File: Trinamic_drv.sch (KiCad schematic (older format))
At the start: 26 parts

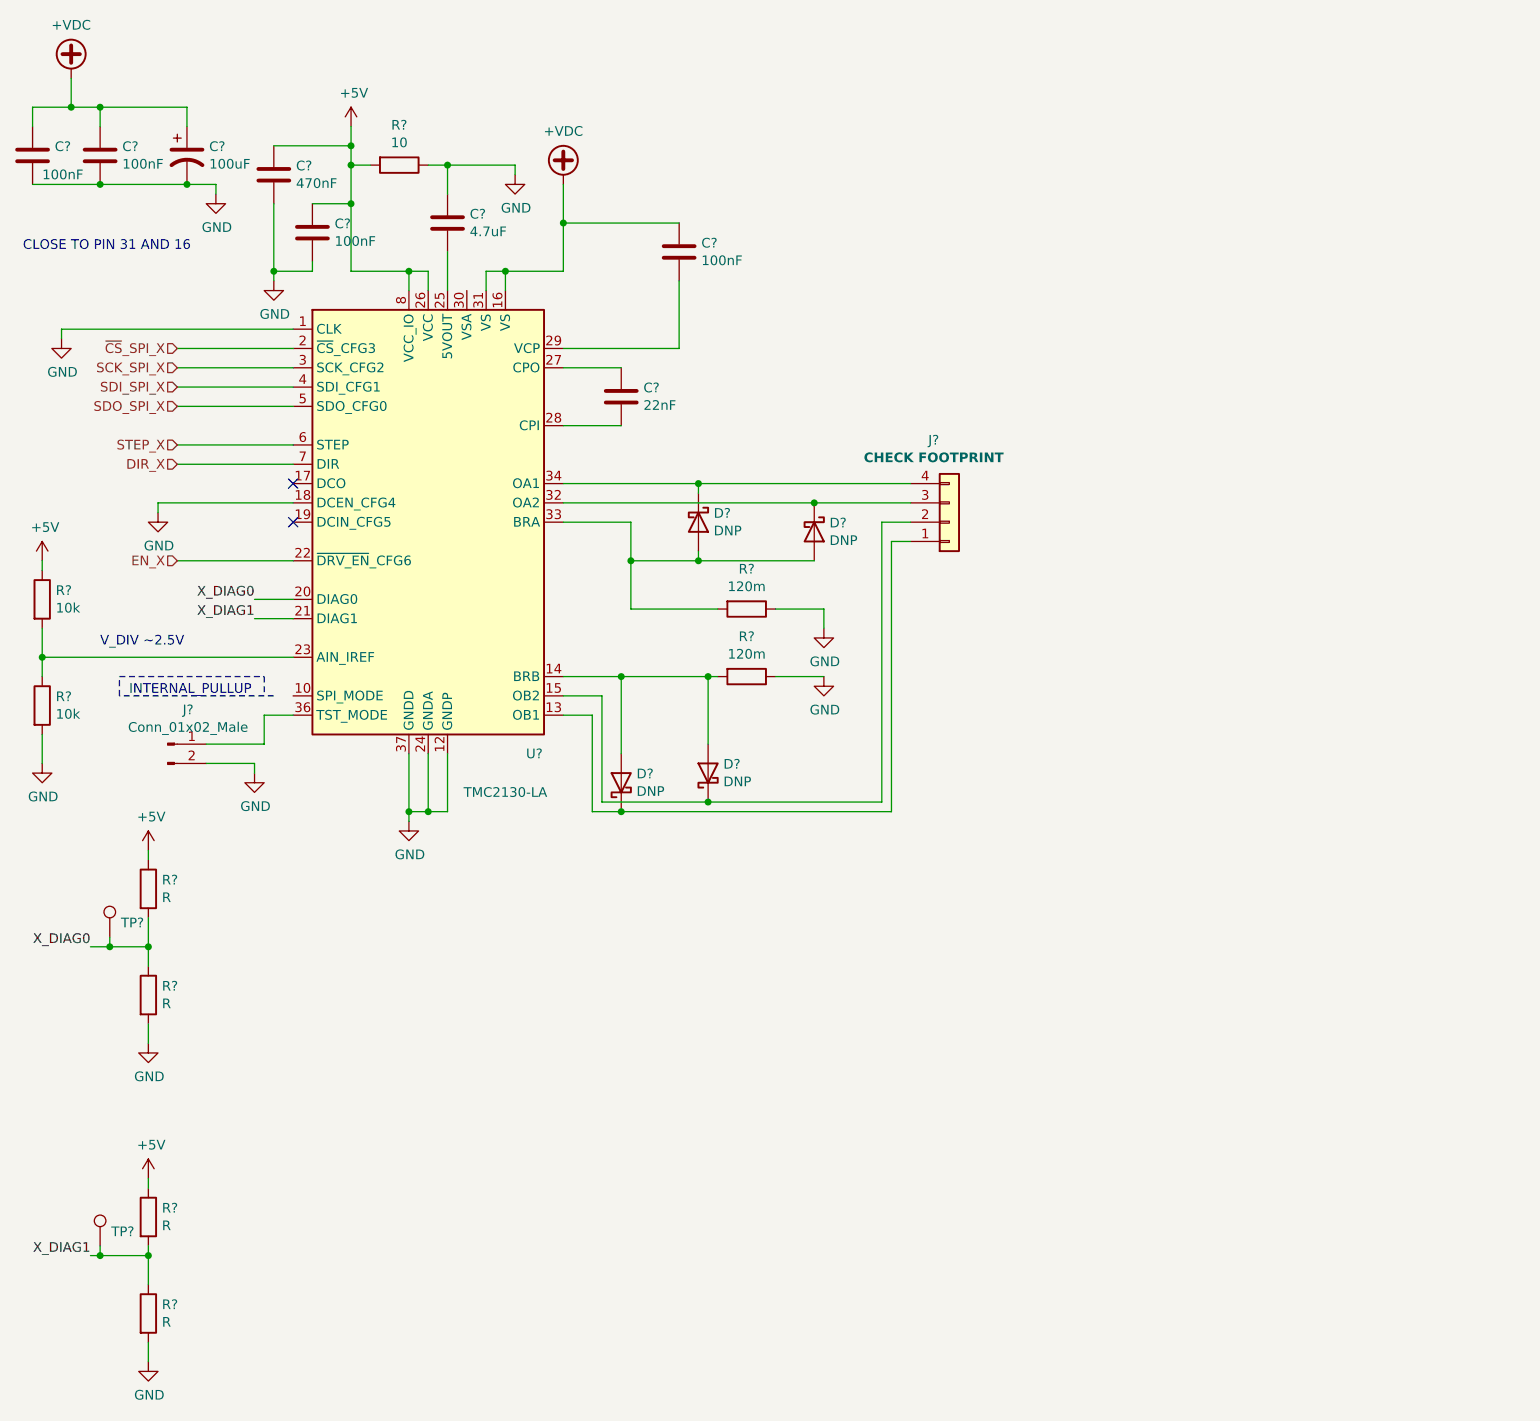
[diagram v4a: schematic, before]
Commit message: Added all stepper circuits. Adding SPI bus to top level sheet. Opened up layout to check connectivity. Errors with footprint libs
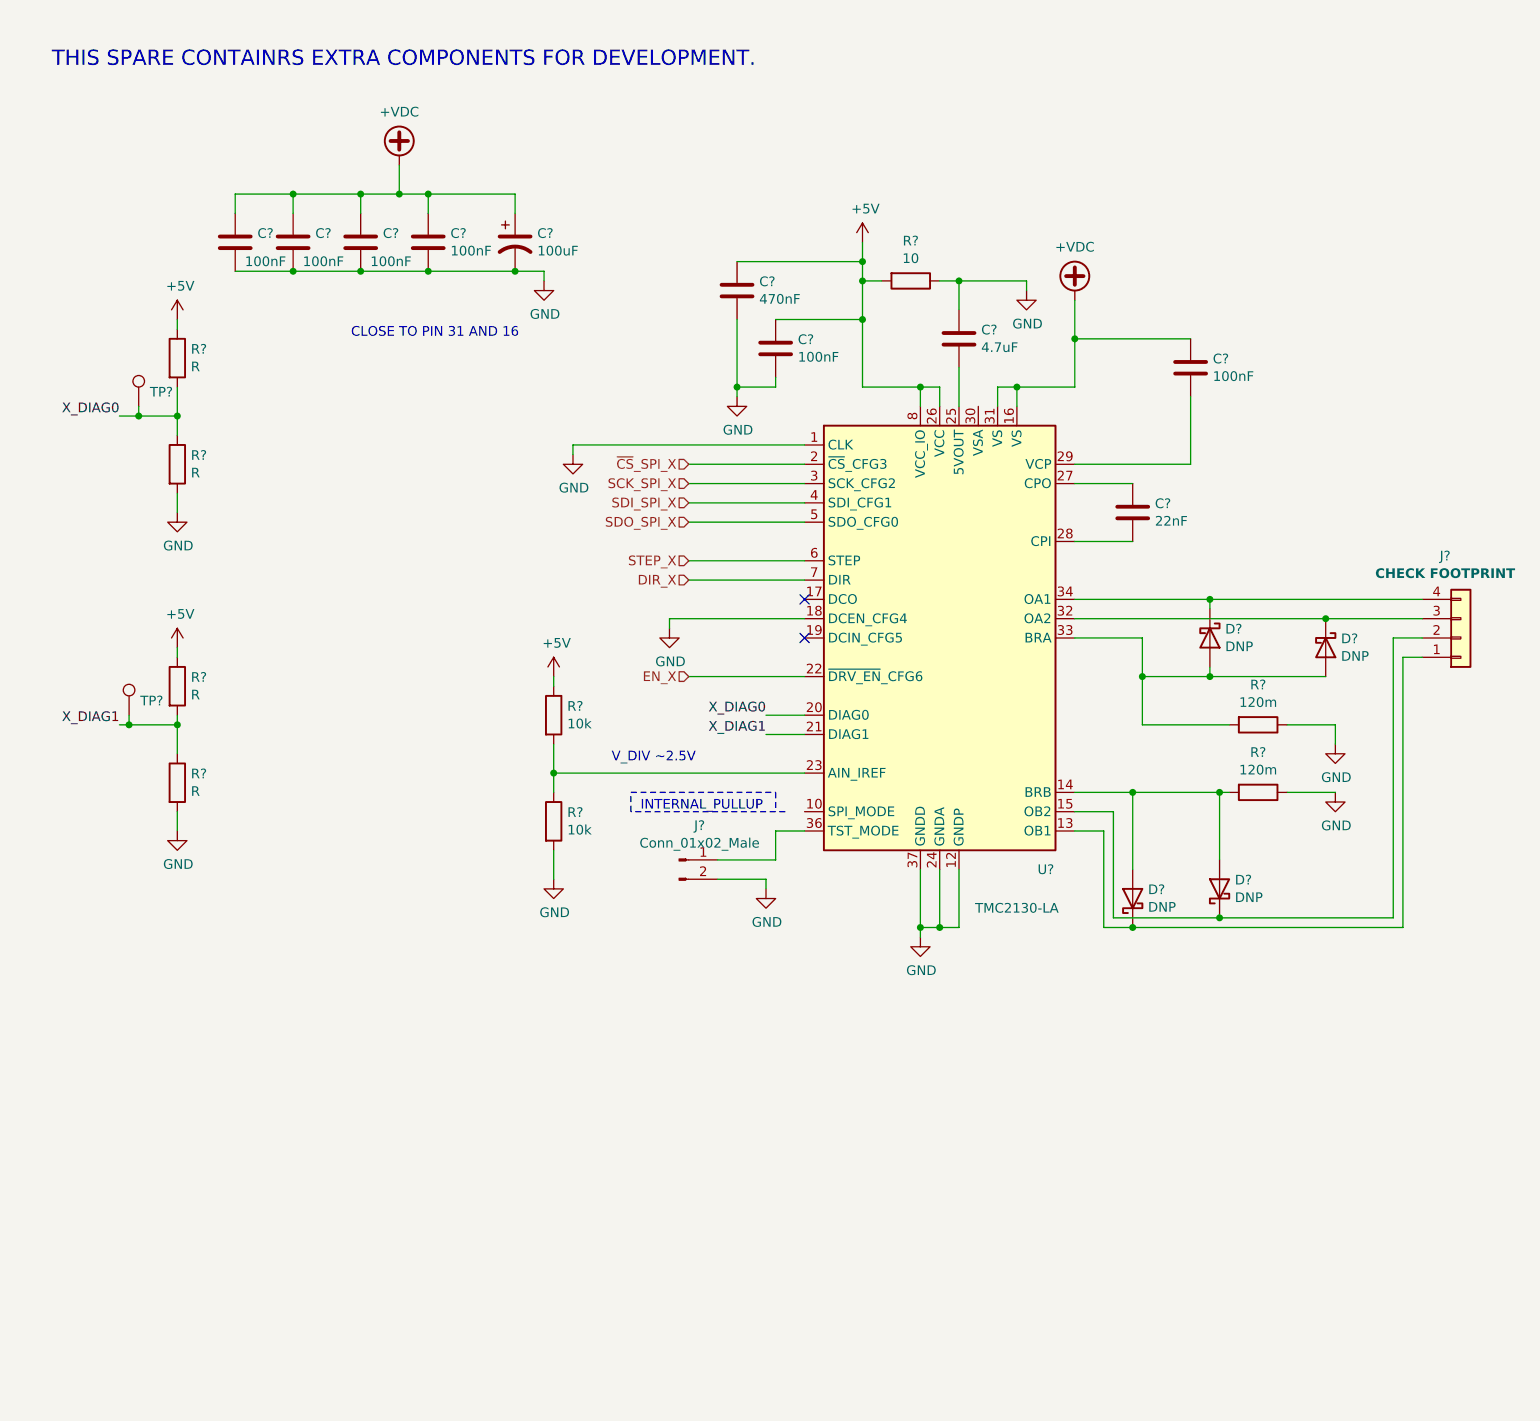
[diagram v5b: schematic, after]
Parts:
- removed R? (x3): R, symbol Device:R
- added C? (x2): 100nF, Capacitors_SMD:C_0805_HandSoldering, symbol Device:C
- added R? (x3): R, Resistor_SMD:R_0805_2012Metric_Pad1.15x1.40mm_HandSolder, symbol Device:R
- R?: footprint (none) -> Resistor_SMD:R_0805_2012Metric_Pad1.15x1.40mm_HandSolder
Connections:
- net +5V: now also R?.1
- net +VDC: now also C?.1, C?.1
- net GND: now also C?.2, C?.2, R?.2, R?.2
- net X_DIAG0: now also R?.1
- net X_DIAG1: now also R?.1, R?.2
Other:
- note added: "THIS SPARE CONTAINRS EXTRA COMPONENTS FOR DEVELOPMENT."
- moved on the sheet: C?, D?, J?, R?, TP?, U?
